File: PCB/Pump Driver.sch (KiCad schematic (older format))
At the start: 44 parts, among them P1 CONN_13X2, P10 CONN_2, P11 CONN_2, P12 CONN_2, P2 CONN_9, P3 CONN_2, P4 CONN_2, P5 CONN_2, P6 CONN_2, P7 CONN_2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

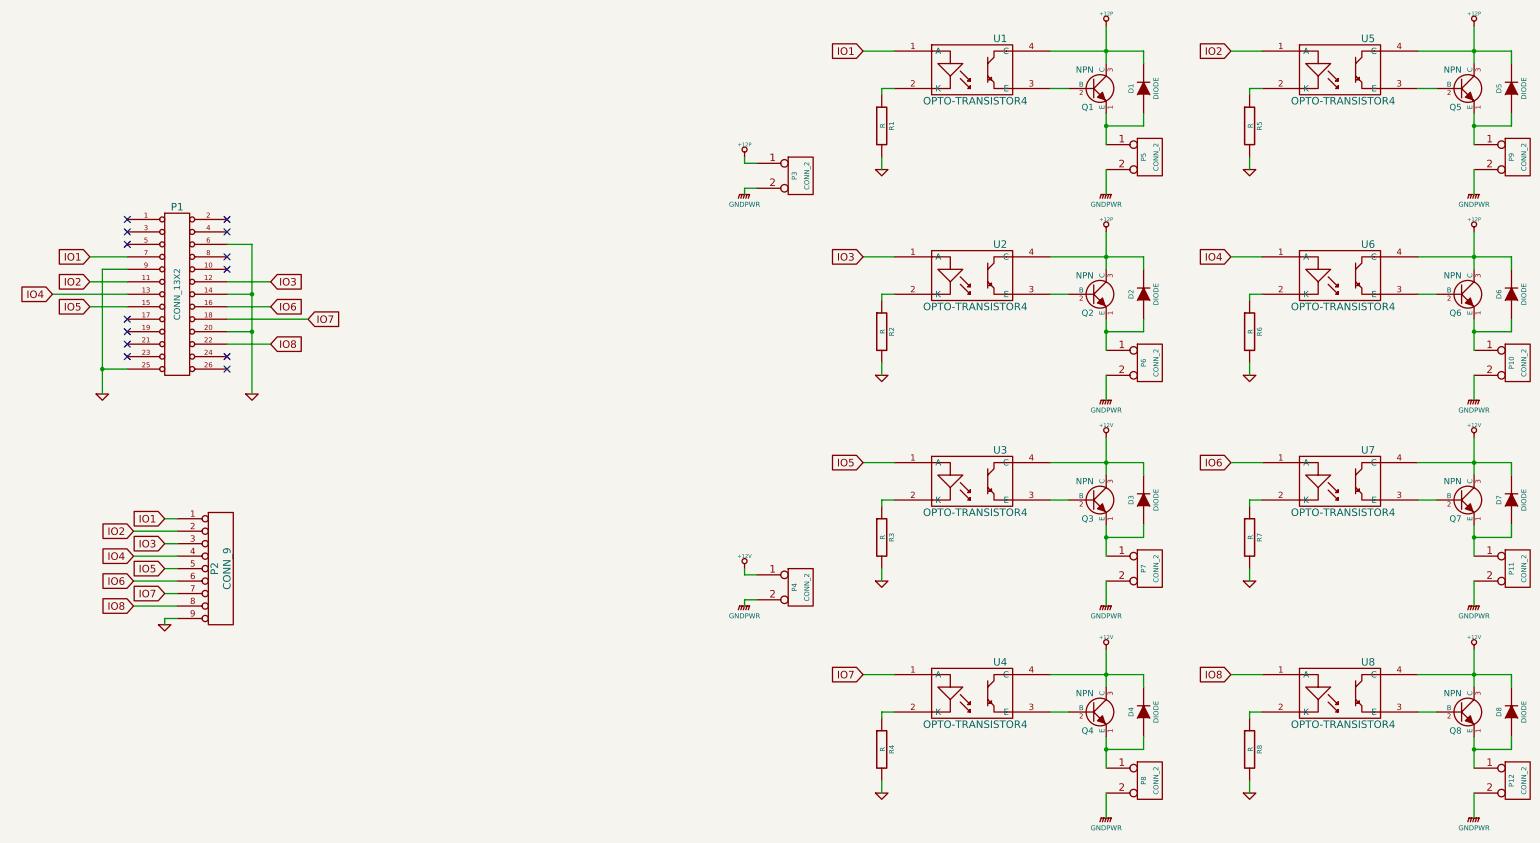
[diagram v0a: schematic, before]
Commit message: Update schematic and start PCB layout
Update schematic with part values and numbers, create netlist and part
footprints, start component layout.
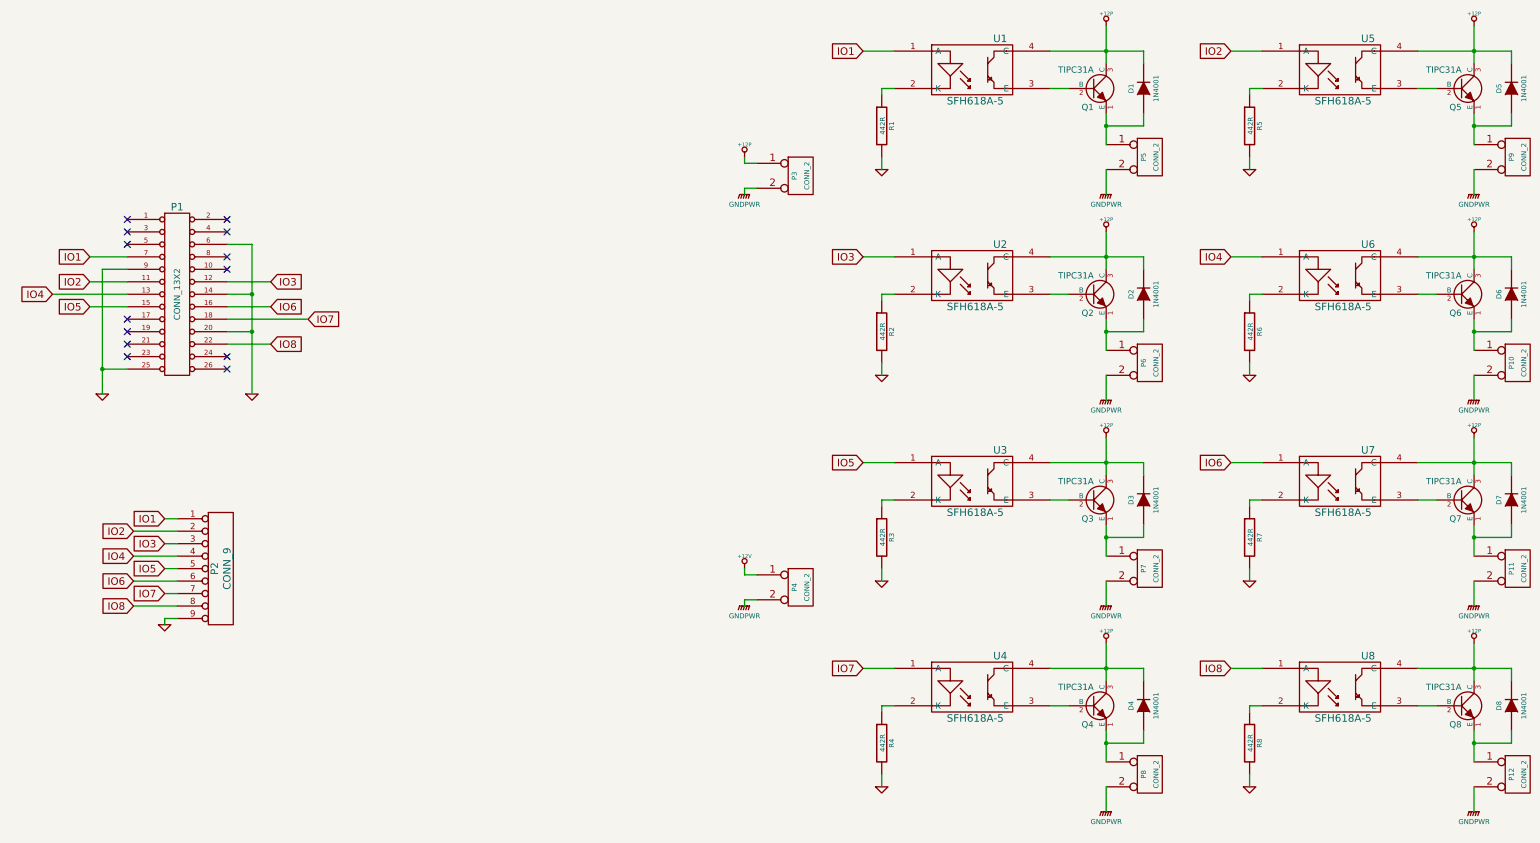
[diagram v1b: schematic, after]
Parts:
- D1, D2, D3, D4, D5, D6, D7, D8: value DIODE -> 1N4001; Link to Component (none) -> http://au.element14.com/micro-commercial-components/1n4001-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
- P1: Link to Component (none) -> http://au.element14.com/3m/30326-6002hb/wire-to-board-conn-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
- P10, P11, P12, P3, P4, P5, P6, P7, P8, P9: Link to Component (none) -> http://au.element14.com/multicomp/eb3-02-b-180/terminal-blo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; Matching Connector (none) -> http://au.element14.com/multicomp/ebk-02-b/terminal-block-e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
- Q1, Q2, Q3, Q4, Q5, Q6, Q7, Q8: value NPN -> TIPC31A; Link to Component (none) -> http://au.element14.com/multicomp/tip31a/transistor-npn-to-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
- R1, R2, R3, R4, R5, R6, R7, R8: value R -> 442R; Link to Component (none) -> http://au.element14.com/vishay-bc-components/mrs25000c4420f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
- U1, U2, U3, U4, U5, U6, U7, U8: value OPTO-TRANSISTOR4 -> SFH618A-5; Link to Component (none) -> http://au.element14.com/vishay-semiconductor/sfh618a-5/opto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
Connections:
- net +12P: now also D3.2 (K), D4.2 (K), D7.2 (K), D8.2 (K), Q3.3 (C), Q4.3 (C), Q7.3 (C), Q8.3 (C), U3.4 (C), U4.4 (C), U7.4 (C), U8.4 (C)
- net +12V: no longer D3.2 (K), D4.2 (K), D7.2 (K), D8.2 (K), Q3.3 (C), Q4.3 (C), Q7.3 (C), Q8.3 (C), U3.4 (C), U4.4 (C), U7.4 (C), U8.4 (C)

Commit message: Lay all tracks & ground plane. Correct schematic
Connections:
- net +12P: no longer D3.2 (K), D4.2 (K), D7.2 (K), D8.2 (K), Q3.3 (C), Q4.3 (C), Q7.3 (C), Q8.3 (C), U3.4 (C), U4.4 (C), U7.4 (C), U8.4 (C)
- net +12V: now also D3.2 (K), D4.2 (K), D7.2 (K), D8.2 (K), Q3.3 (C), Q4.3 (C), Q7.3 (C), Q8.3 (C), U3.4 (C), U4.4 (C), U7.4 (C), U8.4 (C)
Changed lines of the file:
@@
 Sheet 1 1
 Title "Isolated Pump Driver"
-Date "18 jun 2014"
+Date "20 jun 2014"
 Rev "0.1"
 Comp "Studio CM"
@@
 	9450 7750 9700 7750
 $Comp
-L +12P #PWR028
-U 1 1 53A01B54
-P 11400 5900
-F 0 "#PWR028" H 11400 5870 30  0001 C CNN
-F 1 "+12P" H 11400 6000 30  0000 C CNN
-F 2 "" H 11400 5900 60  0000 C CNN
-F 3 "" H 11400 5900 60  0000 C CNN
-	1    11400 5900
-	1    0    0    -1
-$EndComp
-$Comp
-L +12P #PWR029
-U 1 1 53A01B5A
-P 14350 5900
-F 0 "#PWR029" H 14350 5870 30  0001 C CNN
-F 1 "+12P" H 14350 6000 30  0000 C CNN
-F 2 "" H 14350 5900 60  0000 C CNN
-F 3 "" H 14350 5900 60  0000 C CNN
-	1    14350 5900
-	1    0    0    -1
-$EndComp
-$Comp
-L +12P #PWR030
-U 1 1 53A01B60
-P 14350 7550
-F 0 "#PWR030" H 14350 7520 30  0001 C CNN
-F 1 "+12P" H 14350 7650 30  0000 C CNN
-F 2 "" H 14350 7550 60  0000 C CNN
-F 3 "" H 14350 7550 60  0000 C CNN
-	1    14350 7550
-	1    0    0    -1
-$EndComp
-$Comp
-L +12P #PWR031
-U 1 1 53A01B66
-P 11400 7550
-F 0 "#PWR031" H 11400 7520 30  0001 C CNN
-F 1 "+12P" H 11400 7650 30  0000 C CNN
-F 2 "" H 11400 7550 60  0000 C CNN
-F 3 "" H 11400 7550 60  0000 C CNN
-	1    11400 7550
-	1    0    0    -1
-$EndComp
-$Comp
 L NPN Q3
 U 1 1 53A01B6D
@@
 	1    0    0    -1
 $EndComp
+$Comp
+L +12V #PWR?
+U 1 1 53A4310C
+P 11400 5900
+F 0 "#PWR?" H 11400 5850 20  0001 C CNN
+F 1 "+12V" H 11400 6000 30  0000 C CNN
+F 2 "" H 11400 5900 60  0000 C CNN
+F 3 "" H 11400 5900 60  0000 C CNN
+	1    11400 5900
+	1    0    0    -1
+$EndComp
+$Comp
+L +12V #PWR?
+U 1 1 53A43112
+P 14350 5900
+F 0 "#PWR?" H 14350 5850 20  0001 C CNN
+F 1 "+12V" H 14350 6000 30  0000 C CNN
+F 2 "" H 14350 5900 60  0000 C CNN
+F 3 "" H 14350 5900 60  0000 C CNN
+	1    14350 5900
+	1    0    0    -1
+$EndComp
+$Comp
+L +12V #PWR?
+U 1 1 53A43118
+P 11400 7550
+F 0 "#PWR?" H 11400 7500 20  0001 C CNN
+F 1 "+12V" H 11400 7650 30  0000 C CNN
+F 2 "" H 11400 7550 60  0000 C CNN
+F 3 "" H 11400 7550 60  0000 C CNN
+	1    11400 7550
+	1    0    0    -1
+$EndComp
+$Comp
+L +12V #PWR?
+U 1 1 53A4311E
+P 14350 7550
+F 0 "#PWR?" H 14350 7500 20  0001 C CNN
+F 1 "+12V" H 14350 7650 30  0000 C CNN
+F 2 "" H 14350 7550 60  0000 C CNN
+F 3 "" H 14350 7550 60  0000 C CNN
+	1    14350 7550
+	1    0    0    -1
+$EndComp
